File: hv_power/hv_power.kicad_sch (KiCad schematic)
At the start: 9 parts, among them J13 Conn_02x04_Odd_Even, J14 Conn_01x01_Male

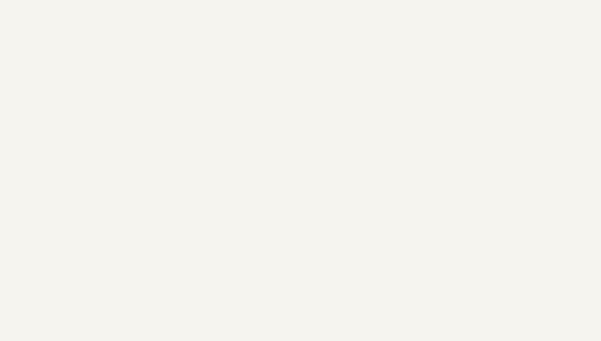
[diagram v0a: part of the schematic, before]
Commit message: Moving to new CCU8 implementation. Moved trace and @arm scripts to octave archive.
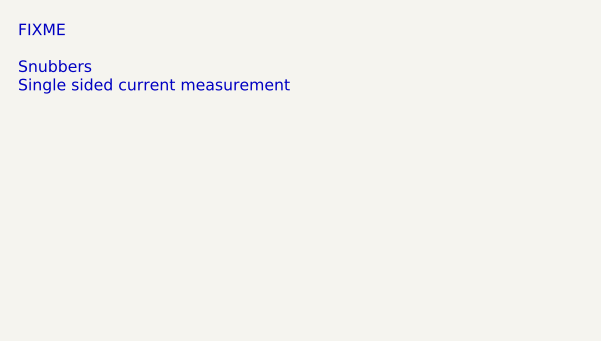
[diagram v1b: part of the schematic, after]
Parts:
- J13: Manufacturer Samtec -> (none)
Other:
- note added: "FIXME Snubbers Single sided current measurement"
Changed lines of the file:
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@@
-(kicad_sch (version 20201015) (generator eeschema)
+(kicad_sch (version 20210126) (generator eeschema)
   (paper "A4")
   (junction (at 82.55 93.98) (diameter 1.016) (color 0 0 0 0))
@@
     (stroke (width 0) (type solid) (color 0 0 0 0))
   )
+  (text "FIXME\n\nSnubbers\nSingle sided current measurement" (at 45.72 29.21 0)
+    (effects (font (size 1.27 1.27)) (justify left bottom))
+  )
   (label "HBL2" (at 82.55 125.73 90)
     (effects (font (size 1.27 1.27)) (justify left bottom))
@@
       (effects (font (size 1.524 1.524)))
     )
+    (pin "1")
   )
   (symbol (lib_id "Local:+797V") (at 193.04 41.91 0) (unit 1)
@@
       (effects (font (size 1.27 1.27)) hide)
     )
+    (pin "1")
   )
   (symbol (lib_id "Local:+800V") (at 217.17 137.16 180) (unit 1)
@@
       (effects (font (size 1.27 1.27)) hide)
     )
+    (pin "1")
   )
   (symbol (lib_id "Connector:Conn_01x01_Male") (at 184.15 44.45 0) (unit 1)
@@
       (effects (font (size 1.27 1.27)) hide)
     )
+    (pin "1")
   )
   (symbol (lib_id "Device:C") (at 199.39 130.81 0) (unit 1)
@@
       (effects (font (size 1.27 1.27)) hide)
     )
+    (pin "1")
+    (pin "2")
   )
   (symbol (lib_id "Device:C") (at 217.17 130.81 0) (unit 1)
@@
       (effects (font (size 1.27 1.27)) hide)
     )
+    (pin "1")
+    (pin "2")
   )
   (symbol (lib_id "Local:NTC") (at 90.17 86.36 0) (unit 1)
@@
       (effects (font (size 1.524 1.524)))
     )
+    (pin "1")
+    (pin "2")
   )
   (symbol (lib_id "Local:HOLE") (at 199.39 113.03 0) (unit 1)
@@
       (effects (font (size 1.524 1.524)))
     )
+    (pin "1")
   )
   (symbol (lib_id "Local:HOLE") (at 208.28 113.03 0) (unit 1)
@@
       (effects (font (size 1.524 1.524)))
     )
+    (pin "1")
   )
   (symbol (lib_id "Local:HOLE") (at 217.17 113.03 0) (unit 1)
@@
       (effects (font (size 1.524 1.524)))
     )
+    (pin "1")
   )
   (symbol (lib_id "Local:HOLE") (at 226.06 113.03 0) (unit 1)
@@
       (effects (font (size 1.524 1.524)))
     )
+    (pin "1")
   )
   (symbol (lib_id "Connector_Generic:Conn_02x04_Odd_Even") (at 85.09 102.87 90) (unit 1)
@@
       (effects (font (size 1.27 1.27)) hide)
     )
-    (property "Manufacturer" "Samtec" (id 4) (at 85.09 102.87 0)
-      (effects (font (size 1.27 1.27)) hide)
-    )
     (property "Mouser" "200-FTM10402LDV" (id 5) (at 85.09 102.87 0)
       (effects (font (size 1.27 1.27)) hide)
@@
       (effects (font (size 1.27 1.27)) hide)
     )
+    (pin "1")
+    (pin "2")
+    (pin "3")
+    (pin "4")
+    (pin "5")
+    (pin "6")
+    (pin "7")
+    (pin "8")
   )
   (sheet (at 139.7 69.85) (size 20.32 20.32)

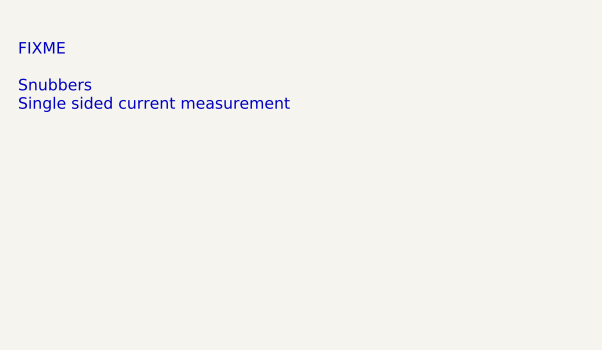
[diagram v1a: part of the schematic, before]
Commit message: All half-bridges work.
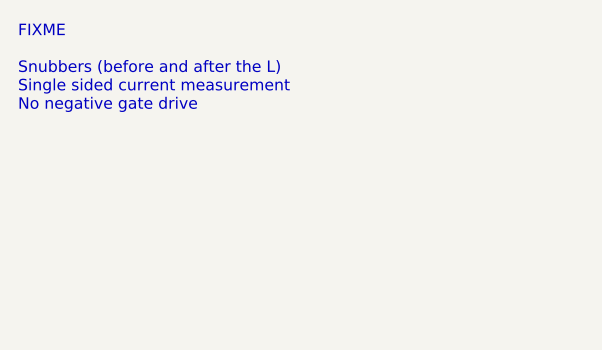
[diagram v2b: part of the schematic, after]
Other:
- note added: "FIXME Snubbers (before and after the L) Single sided current measurement No negative gate drive"
- note removed: "FIXME Snubbers Single sided current measurement"
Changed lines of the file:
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@@
     (stroke (width 0) (type solid) (color 0 0 0 0))
   )
-  (text "FIXME\n\nSnubbers\nSingle sided current measurement" (at 45.72 29.21 0)
+  (text "FIXME\n\nSnubbers (before and after the L)\nSingle sided current measurement\nNo negative gate drive"
+    (at 45.72 29.21 0)
     (effects (font (size 1.27 1.27)) (justify left bottom))
   )

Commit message: Ordered new boards.
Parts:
- removed J14: Conn_01x01_Male, TestPoint:TestPoint_Pad_1.0x1.0mm, symbol Connector:Conn_01x01_Male
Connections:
- net pe: now reaches C1.1, C2.1, HOLE1.1, HOLE2.1
- net ntc: now reaches J13.8 (Pin_8), R1.2
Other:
- sheet H_Bridge0 ports: added V_servo; removed none

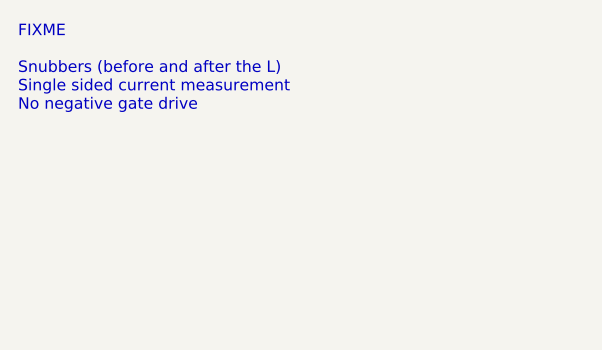
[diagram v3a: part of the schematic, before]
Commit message: Set the run bit in the timer for the POSIF.
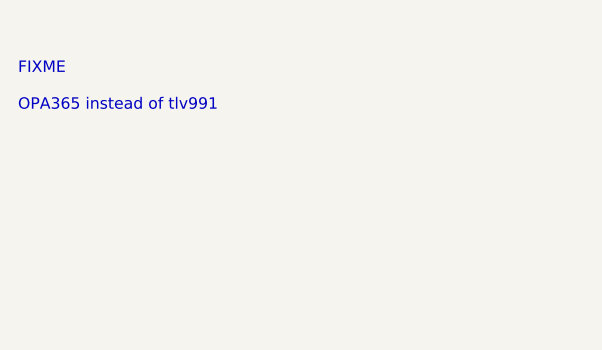
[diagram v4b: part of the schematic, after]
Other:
- note added: "FIXME OPA365 instead of tlv991"
- note removed: "FIXME Snubbers (before and after the L) Single sided current measurement No negative gate drive"
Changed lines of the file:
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@@
     (stroke (width 0) (type solid))
   )
-  (text "FIXME\n\nSnubbers (before and after the L)\nSingle sided current measurement\nNo negative gate drive"
-    (at 45.72 29.21 0)
+  (text "FIXME\n\nOPA365 instead of tlv991" (at 45.72 29.21 0)
     (effects (font (size 1.27 1.27)) (justify left bottom))
   )
